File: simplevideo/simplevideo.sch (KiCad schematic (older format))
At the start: 8 parts, among them Q2 2N3904, U18 74HCT00

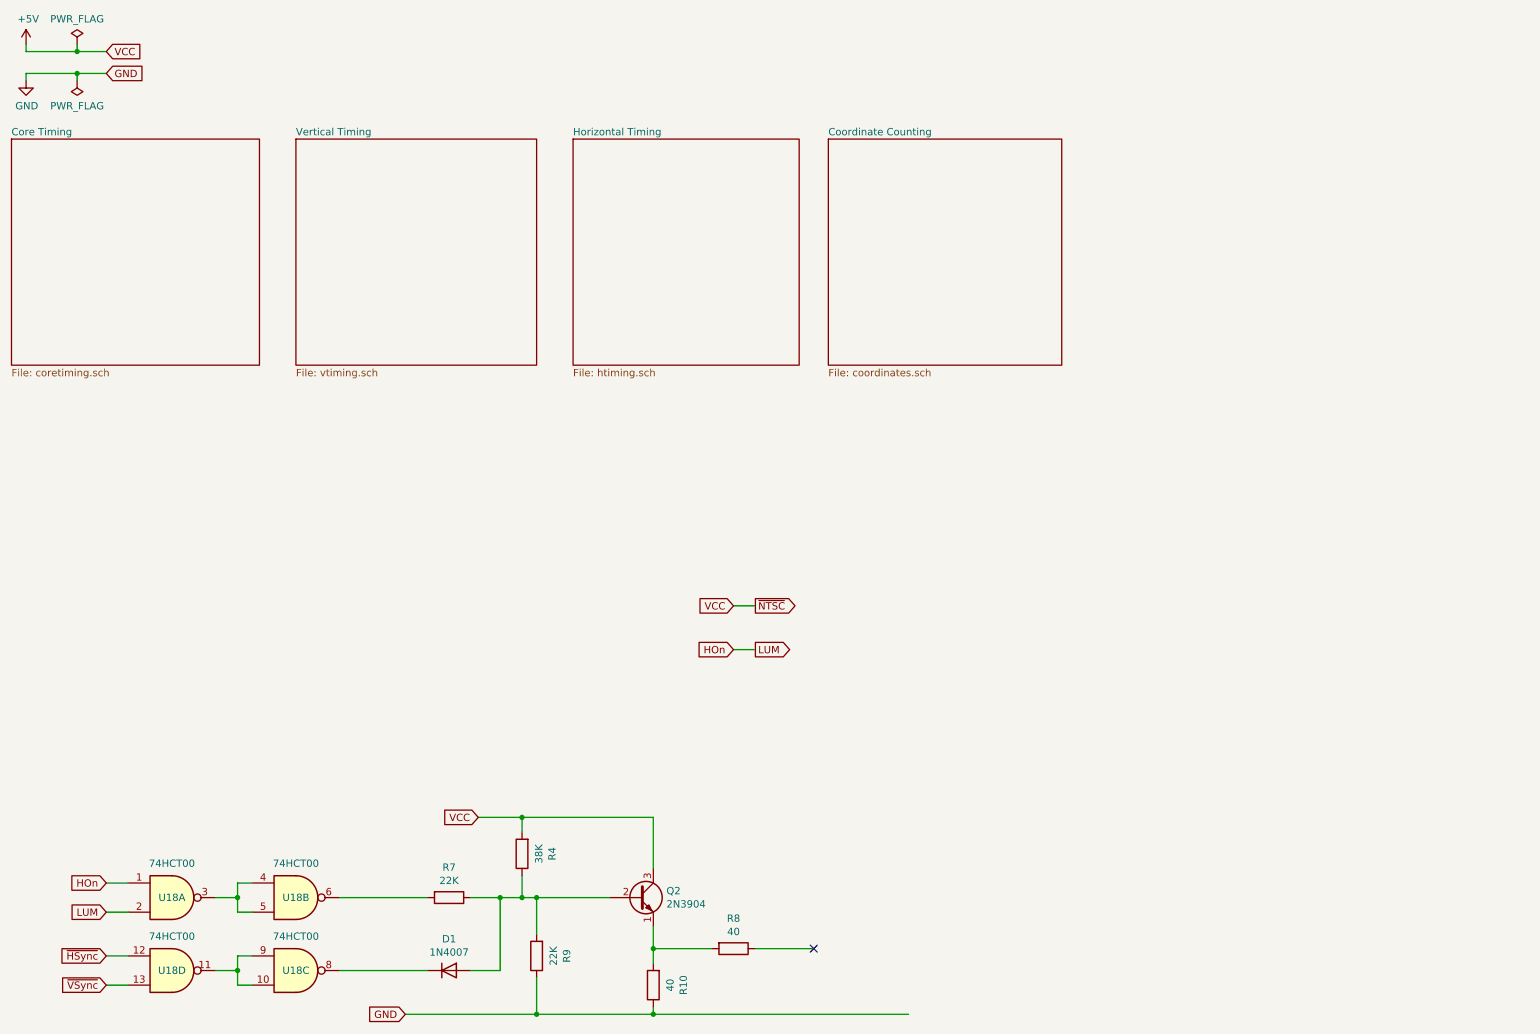
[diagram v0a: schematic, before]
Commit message: Include 6502, ROM, etc in circuit, all laid out together
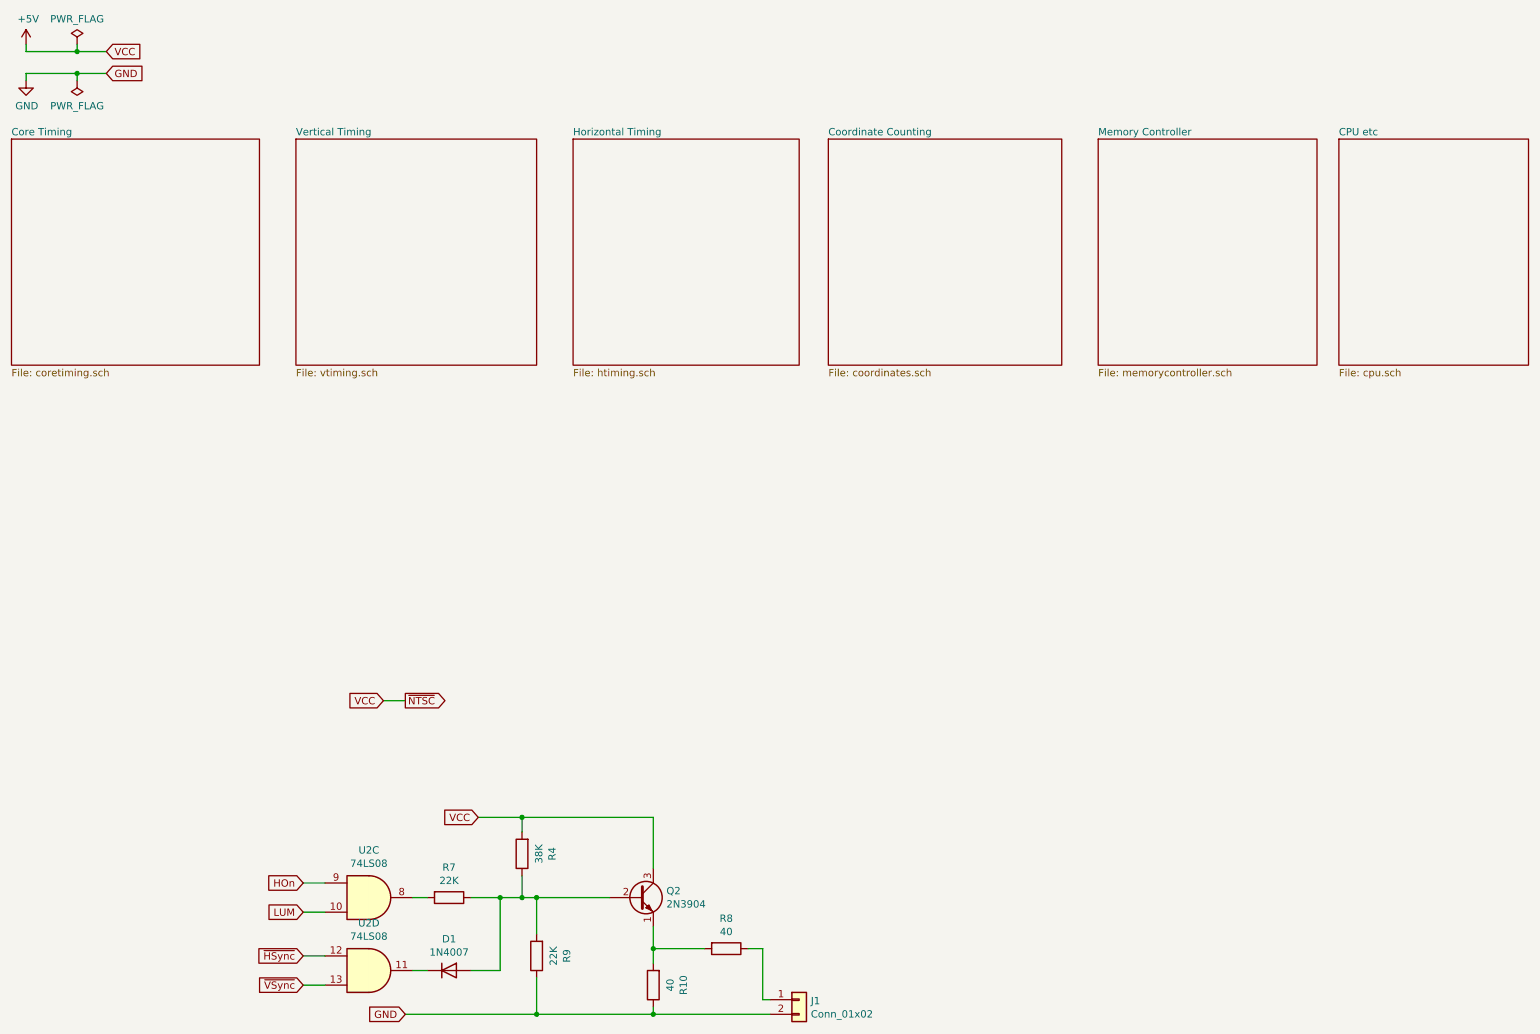
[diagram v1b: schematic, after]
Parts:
- removed U18: 74HCT00, Package_DIP:DIP-14_W7.62mm, symbol 74xx:74HCT00
- added J1: Conn_01x02, Connector_PinHeader_2.54mm:PinHeader_1x02_P2.54mm_Vertical, symbol Connector_Generic:Conn_01x02
- added U2: 74LS08, Package_DIP:DIP-14_W7.62mm, symbol 74xx:74LS08
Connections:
- net GND: now also J1.2 (Pin_2)
- net HOn: now also U2.9
- net ~HSync: now also U2.12
- net ~VSync: now also U2.13
- net at R8.1: now also J1.1 (Pin_1)
- net at D1.1 (K): now also U2.11
- net at R7.2: now also U2.8
- new net LUM: U2.10
- no-connect marks 1 -> 0
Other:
- moved on the sheet: R8
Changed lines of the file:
@@
 $Descr A4 11693 8268
 encoding utf-8
-Sheet 1 5
+Sheet 1 7
 Title ""
 Date ""
@@
 F1 "htiming.sch" 50
 $EndSheet
-Text GLabel 5650 4750 0    50   Input ~ 0
+Text GLabel 3250 5400 0    50   Input ~ 0
 VCC
-Text GLabel 5800 4750 2    50   Output ~ 0
+Text GLabel 3400 5400 2    50   Output ~ 0
 ~NTSC
 Wire Wire Line
-	5650 4750 5800 4750
+	3250 5400 3400 5400
 $Comp
 L Transistor_BJT:2N3904 Q2
@@
 Text GLabel 3400 7550 0    50   Input ~ 0
 GND
-Text GLabel 1350 7150 0    50   Input ~ 0
+Text GLabel 2700 7150 0    50   Input ~ 0
 ~HSync
-Text GLabel 1350 7350 0    50   Input ~ 0
+Text GLabel 2700 7350 0    50   Input ~ 0
 ~VSync
-$Comp
-L 74xx:74HCT00 U18
-U 4 1 5F235E09
-P 1800 7250
-F 0 "U18" H 1800 7250 50  0000 C CNN
-F 1 "74HCT00" H 1800 7484 50  0000 C CNN
-F 2 "Package_DIP:DIP-14_W7.62mm" H 1800 7250 50  0001 C CNN
-F 3 "http://www.ti.com/lit/gpn/sn74hct00" H 1800 7250 50  0001 C CNN
-	4    1800 7250
-	1    0    0    -1
-$EndComp
-Wire Wire Line
-	1500 7150 1350 7150
-Wire Wire Line
-	1500 7350 1350 7350
-Wire Wire Line
-	2100 7250 2250 7250
+Wire Wire Line
+	2850 7150 2700 7150
+Wire Wire Line
+	2850 7350 2700 7350
 $Comp
 L Device:R R7
@@
 Connection ~ 5100 7550
 Wire Wire Line
-	5100 7550 6850 7550
+	5100 7550 5900 7550
 Wire Wire Line
 	5100 6950 5100 7100
 Wire Wire Line
-	5100 7100 5500 7100
+	5100 7100 5450 7100
 Connection ~ 5100 7100
 Wire Wire Line
@@
 L Device:R R8
 U 1 1 5EDE0EE4
-P 5650 7100
-F 0 "R8" V 5443 7100 50  0000 C CNN
-F 1 "40" V 5534 7100 50  0000 C CNN
-F 2 "Resistor_THT:R_Axial_DIN0204_L3.6mm_D1.6mm_P7.62mm_Horizontal" V 5580 7100 50  0001 C CNN
-F 3 "~" H 5650 7100 50  0001 C CNN
-	1    5650 7100
+P 5600 7100
+F 0 "R8" V 5393 7100 50  0000 C CNN
+F 1 "40" V 5484 7100 50  0000 C CNN
+F 2 "Resistor_THT:R_Axial_DIN0204_L3.6mm_D1.6mm_P7.62mm_Horizontal" V 5530 7100 50  0001 C CNN
+F 3 "~" H 5600 7100 50  0001 C CNN
+	1    5600 7100
 	0    1    1    0
 $EndComp
 Wire Wire Line
-	5800 7100 6200 7100
+	5750 7100 5850 7100
 Wire Wire Line
 	5100 6200 4200 6200
@@
 Text GLabel 3900 6200 0    50   Input ~ 0
 VCC
-$Comp
-L 74xx:74HCT00 U18
-U 3 1 5EDF24F9
-P 2650 7250
-F 0 "U18" H 2650 7250 50  0000 C CNN
-F 1 "74HCT00" H 2650 7484 50  0000 C CNN
-F 2 "Package_DIP:DIP-14_W7.62mm" H 2650 7250 50  0001 C CNN
-F 3 "http://www.ti.com/lit/gpn/sn74hct00" H 2650 7250 50  0001 C CNN
-	3    2650 7250
-	1    0    0    -1
-$EndComp
-Wire Wire Line
-	2350 7350 2250 7350
-Wire Wire Line
-	2250 7350 2250 7250
-Wire Wire Line
-	2250 7150 2350 7150
-Connection ~ 2250 7250
-Wire Wire Line
-	2250 7250 2250 7150
 $Comp
 L Device:R R9
@@
 Wire Wire Line
 	4300 7550 5100 7550
-$Comp
-L 74xx:74HCT00 U18
-U 1 1 5EE0C76E
-P 1800 6750
-F 0 "U18" H 1800 6750 50  0000 C CNN
-F 1 "74HCT00" H 1800 6984 50  0000 C CNN
-F 2 "Package_DIP:DIP-14_W7.62mm" H 1800 6750 50  0001 C CNN
-F 3 "http://www.ti.com/lit/gpn/sn74hct00" H 1800 6750 50  0001 C CNN
-	1    1800 6750
-	1    0    0    -1
-$EndComp
-Wire Wire Line
-	2100 6750 2250 6750
-$Comp
-L 74xx:74HCT00 U18
-U 2 1 5EE0C775
-P 2650 6750
-F 0 "U18" H 2650 6750 50  0000 C CNN
-F 1 "74HCT00" H 2650 6984 50  0000 C CNN
-F 2 "Package_DIP:DIP-14_W7.62mm" H 2650 6750 50  0001 C CNN
-F 3 "http://www.ti.com/lit/gpn/sn74hct00" H 2650 6750 50  0001 C CNN
-	2    2650 6750
-	1    0    0    -1
-$EndComp
-Wire Wire Line
-	2350 6850 2250 6850
-Wire Wire Line
-	2250 6850 2250 6750
-Wire Wire Line
-	2250 6650 2350 6650
-Connection ~ 2250 6750
-Wire Wire Line
-	2250 6750 2250 6650
-Text GLabel 1350 6650 0    50   Input ~ 0
+Text GLabel 2700 6650 0    50   Input ~ 0
 HOn
-Text GLabel 1350 6850 0    50   Input ~ 0
+Text GLabel 2700 6850 0    50   Input ~ 0
 LUM
 Wire Wire Line
-	1350 6650 1500 6650
-Wire Wire Line
-	1350 6850 1500 6850
-Wire Wire Line
-	2950 6750 3550 6750
-Wire Wire Line
-	2950 7250 3550 7250
+	2700 6650 2850 6650
+Wire Wire Line
+	2700 6850 2850 6850
 Wire Wire Line
 	4050 7250 4050 6750
@@
 Wire Wire Line
 	3850 7250 4050 7250
-Wire Wire Line
-	5650 5050 5800 5050
-Text GLabel 5650 5050 0    50   Input ~ 0
-HOn
-Text GLabel 5800 5050 2    50   Output ~ 0
-LUM
-NoConn ~ 6200 7100
 $Sheet
 S 6300 1550 1600 1550
@@
 F1 "coordinates.sch" 50
 $EndSheet
+$Sheet
+S 8150 1550 1500 1550
+U 5EE02DBD
+F0 "Memory Controller" 50
+F1 "memorycontroller.sch" 50
+$EndSheet
+$Sheet
+S 9800 1550 1300 1550
+U 5FE807DE
+F0 "CPU etc" 50
+F1 "cpu.sch" 50
+$EndSheet
+$Comp
+L Connector_Generic:Conn_01x02 J1
+U 1 1 5FEC914C
+P 6100 7450
+F 0 "J1" H 6180 7442 50  0000 L CNN
+F 1 "Conn_01x02" H 6180 7351 50  0000 L CNN
+F 2 "Connector_PinHeader_2.54mm:PinHeader_1x02_P2.54mm_Vertical" H 6100 7450 50  0001 C CNN
+F 3 "~" H 6100 7450 50  0001 C CNN
+	1    6100 7450
+	1    0    0    -1
+$EndComp
+Wire Wire Line
+	5900 7450 5850 7450
+Wire Wire Line
+	5850 7450 5850 7100
+$Comp
+L 74xx:74LS08 U2
+U 3 1 5FFB1A37
+P 3150 6750
+F 0 "U2" H 3150 7075 50  0000 C CNN
+F 1 "74LS08" H 3150 6984 50  0000 C CNN
+F 2 "Package_DIP:DIP-14_W7.62mm" H 3150 6750 50  0001 C CNN
+F 3 "http://www.ti.com/lit/gpn/sn74LS08" H 3150 6750 50  0001 C CNN
+	3    3150 6750
+	1    0    0    -1
+$EndComp
+$Comp
+L 74xx:74LS08 U2
+U 4 1 5FFB6050
+P 3150 7250
+F 0 "U2" H 3150 7575 50  0000 C CNN
+F 1 "74LS08" H 3150 7484 50  0000 C CNN
+F 2 "Package_DIP:DIP-14_W7.62mm" H 3150 7250 50  0001 C CNN
+F 3 "http://www.ti.com/lit/gpn/sn74LS08" H 3150 7250 50  0001 C CNN
+	4    3150 7250
+	1    0    0    -1
+$EndComp
+Wire Wire Line
+	3450 7250 3550 7250
+Wire Wire Line
+	3450 6750 3550 6750
 $EndSCHEMATC

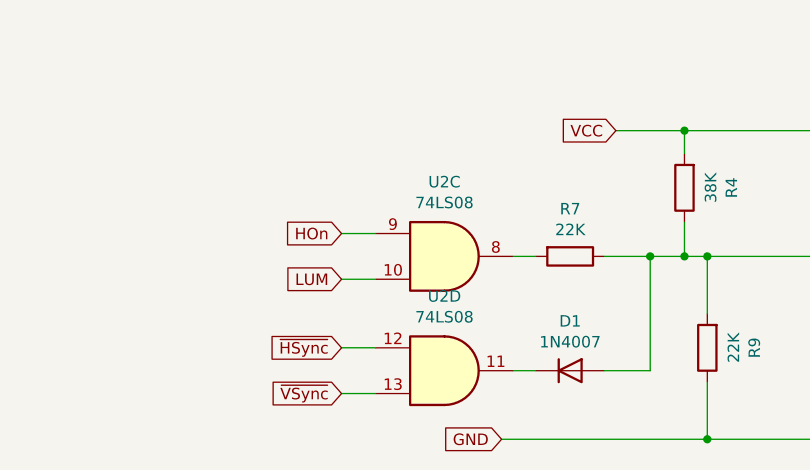
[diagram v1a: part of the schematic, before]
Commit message: New address decoding scheme and complete breadboard layout, should be ready to build
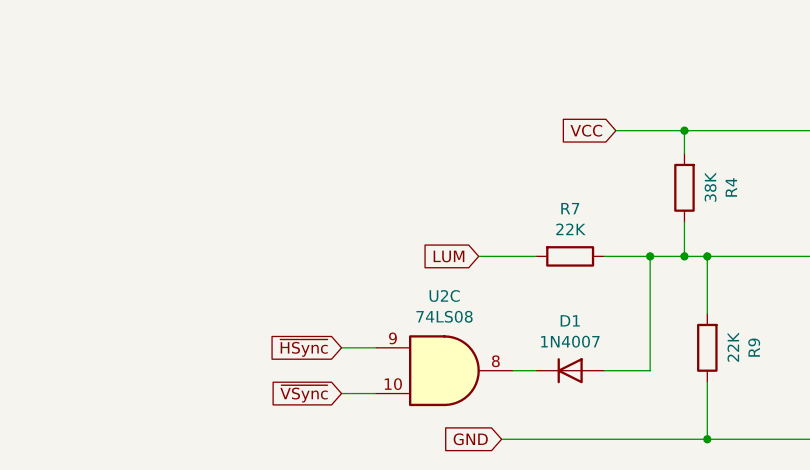
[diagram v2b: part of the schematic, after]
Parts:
- removed unit 3 of U2
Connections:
- net LUM: now also R7.2
- net ~HSync: now also U2.9; no longer U2.12
- net ~VSync: now also U2.10; no longer U2.13
- net at D1.1 (K): now also U2.8; no longer U2.11
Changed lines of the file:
@@
 Wire Wire Line
 	4300 7550 5100 7550
-Text GLabel 2700 6650 0    50   Input ~ 0
-HOn
-Text GLabel 2700 6850 0    50   Input ~ 0
+Text GLabel 3300 6750 0    50   Input ~ 0
 LUM
-Wire Wire Line
-	2700 6650 2850 6650
-Wire Wire Line
-	2700 6850 2850 6850
 Wire Wire Line
 	4050 7250 4050 6750
@@
 $Comp
 L 74xx:74LS08 U2
-U 3 1 5FFB1A37
-P 3150 6750
-F 0 "U2" H 3150 7075 50  0000 C CNN
-F 1 "74LS08" H 3150 6984 50  0000 C CNN
-F 2 "Package_DIP:DIP-14_W7.62mm" H 3150 6750 50  0001 C CNN
-F 3 "http://www.ti.com/lit/gpn/sn74LS08" H 3150 6750 50  0001 C CNN
-	3    3150 6750
-	1    0    0    -1
-$EndComp
-$Comp
-L 74xx:74LS08 U2
-U 4 1 5FFB6050
+U 3 1 5FFB6050
 P 3150 7250
 F 0 "U2" H 3150 7575 50  0000 C CNN
@@
 F 2 "Package_DIP:DIP-14_W7.62mm" H 3150 7250 50  0001 C CNN
 F 3 "http://www.ti.com/lit/gpn/sn74LS08" H 3150 7250 50  0001 C CNN
-	4    3150 7250
+	3    3150 7250
 	1    0    0    -1
 $EndComp
@@
 	3450 7250 3550 7250
 Wire Wire Line
-	3450 6750 3550 6750
+	3300 6750 3550 6750
 $EndSCHEMATC

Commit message: Minor edits
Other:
- note added: "Composite video output"
- note added: "NTSC vs PAL option"
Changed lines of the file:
@@
 L power:+5V #PWR0107
 U 1 1 5EE1CCD9
-P 800 900
-F 0 "#PWR0107" H 800 750 50  0001 C CNN
-F 1 "+5V" H 815 1073 50  0000 C CNN
-F 2 "" H 800 900 50  0001 C CNN
-F 3 "" H 800 900 50  0001 C CNN
-	1    800  900
-	1    0    0    -1
-$EndComp
-Wire Wire Line
-	800  900  800  950
+P 1450 4500
+F 0 "#PWR0107" H 1450 4350 50  0001 C CNN
+F 1 "+5V" H 1465 4673 50  0000 C CNN
+F 2 "" H 1450 4500 50  0001 C CNN
+F 3 "" H 1450 4500 50  0001 C CNN
+	1    1450 4500
+	1    0    0    -1
+$EndComp
+Wire Wire Line
+	1450 4500 1450 4550
 $Comp
 L power:GND #PWR0109
 U 1 1 5EE2B00E
-P 800 1150
-F 0 "#PWR0109" H 800 900 50  0001 C CNN
-F 1 "GND" H 805 977 50  0000 C CNN
-F 2 "" H 800 1150 50  0001 C CNN
-F 3 "" H 800 1150 50  0001 C CNN
-	1    800  1150
-	1    0    0    -1
-$EndComp
-Wire Wire Line
-	800  1150 800  1100
-Wire Wire Line
-	800  1100 1150 1100
+P 1450 4750
+F 0 "#PWR0109" H 1450 4500 50  0001 C CNN
+F 1 "GND" H 1455 4577 50  0000 C CNN
+F 2 "" H 1450 4750 50  0001 C CNN
+F 3 "" H 1450 4750 50  0001 C CNN
+	1    1450 4750
+	1    0    0    -1
+$EndComp
+Wire Wire Line
+	1450 4750 1450 4700
+Wire Wire Line
+	1450 4700 1800 4700
 $Sheet
 S 700  1550 1700 1550
@@
 F1 "coretiming.sch" 50
 $EndSheet
-Text GLabel 1350 950  2    50   Input ~ 0
+Text GLabel 2000 4550 2    50   Input ~ 0
 VCC
-Text GLabel 1350 1100 2    50   Input ~ 0
+Text GLabel 2000 4700 2    50   Input ~ 0
 GND
 $Comp
 L power:PWR_FLAG #FLG01
 U 1 1 5F2EA31D
-P 1150 900
-F 0 "#FLG01" H 1150 975 50  0001 C CNN
-F 1 "PWR_FLAG" H 1150 1073 50  0000 C CNN
-F 2 "" H 1150 900 50  0001 C CNN
-F 3 "~" H 1150 900 50  0001 C CNN
-	1    1150 900
-	1    0    0    -1
-$EndComp
-Wire Wire Line
-	800  950  1150 950
-Wire Wire Line
-	1150 900  1150 950
-Connection ~ 1150 950
-Wire Wire Line
-	1150 950  1350 950
+P 1800 4500
+F 0 "#FLG01" H 1800 4575 50  0001 C CNN
+F 1 "PWR_FLAG" H 1800 4673 50  0000 C CNN
+F 2 "" H 1800 4500 50  0001 C CNN
+F 3 "~" H 1800 4500 50  0001 C CNN
+	1    1800 4500
+	1    0    0    -1
+$EndComp
+Wire Wire Line
+	1450 4550 1800 4550
+Wire Wire Line
+	1800 4500 1800 4550
+Connection ~ 1800 4550
+Wire Wire Line
+	1800 4550 2000 4550
 $Comp
 L power:PWR_FLAG #FLG02
 U 1 1 5F2EAEF3
-P 1150 1150
-F 0 "#FLG02" H 1150 1225 50  0001 C CNN
-F 1 "PWR_FLAG" H 1150 1323 50  0000 C CNN
-F 2 "" H 1150 1150 50  0001 C CNN
-F 3 "~" H 1150 1150 50  0001 C CNN
-	1    1150 1150
-	-1   0    0    1
-$EndComp
-Wire Wire Line
-	1150 1150 1150 1100
-Connection ~ 1150 1100
-Wire Wire Line
-	1150 1100 1350 1100
+P 1800 4750
+F 0 "#FLG02" H 1800 4825 50  0001 C CNN
+F 1 "PWR_FLAG" H 1800 4923 50  0000 C CNN
+F 2 "" H 1800 4750 50  0001 C CNN
+F 3 "~" H 1800 4750 50  0001 C CNN
+	1    1800 4750
+	-1   0    0    1
+$EndComp
+Wire Wire Line
+	1800 4750 1800 4700
+Connection ~ 1800 4700
+Wire Wire Line
+	1800 4700 2000 4700
 $Sheet
 S 2650 1550 1650 1550
@@
 F1 "htiming.sch" 50
 $EndSheet
-Text GLabel 3250 5400 0    50   Input ~ 0
+Text GLabel 4200 4650 0    50   Input ~ 0
 VCC
-Text GLabel 3400 5400 2    50   Output ~ 0
+Text GLabel 4350 4650 2    50   Output ~ 0
 ~NTSC
 Wire Wire Line
-	3250 5400 3400 5400
+	4200 4650 4350 4650
 $Comp
 L Transistor_BJT:2N3904 Q2
@@
 Wire Wire Line
 	3300 6750 3550 6750
+Text Notes 3950 4500 0    50   ~ 0
+NTSC vs PAL option
+Text Notes 3800 5950 0    50   ~ 0
+Composite video output
 $EndSCHEMATC

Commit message: Fixed various issues discovered during building and testing
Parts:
- removed Q2: 2N3904, Package_TO_SOT_THT:TO-92_Inline, symbol Transistor_BJT:2N3904
- removed U2: 74LS08, Package_DIP:DIP-14_W7.62mm, symbol 74xx:74LS08
- added C10, C11, C2, C3, C4, C5, C6, C7, C8, C9: 220u, Capacitor_THT:CP_Radial_D5.0mm_P2.50mm, symbol Device:CP
- added D4: 1N4148, Diode_THT:D_DO-34_SOD68_P7.62mm_Horizontal, symbol Diode:1N4007
- D1: value 1N4007 -> 1N4148
- R10: value 40 -> 47
- R4: value 38K -> 330
- R7: value 22K -> 200
- R8: value 40 -> 20
- R9: value 22K -> 2K2
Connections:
- net +5V: now also R4.1, R9.1, C10.1, C11.1, C2.1, C3.1, C4.1, C5.1, C6.1, C7.1, C8.1, C9.1; no longer R4.2
- net GND: now also C10.2, C11.2, C2.2, C3.2, C4.2, C5.2, C6.2, C7.2, C8.2, C9.2; no longer R10.1, R9.1
- net ~HSync: now also D1.1 (K)
- net ~VSync: now also D4.1 (K)
- net at R10.2: now also R8.1; no longer R8.2
- net at J1.1 (Pin_1): now also R10.1; no longer R8.1
- net at D1.2 (A), R7.1, R9.2: now also R4.2, R8.2, D4.2 (A); no longer R4.1
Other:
- note added: "75 ohm termination"
- moved on the sheet: D1, J1, R4, R7, R8
